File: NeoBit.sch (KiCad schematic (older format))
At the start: 19 parts, among them J1 AudioJack3_Ground, J2 Barrel_Jack_MountingPin, J3 Qwiic, J4 DotStars, J5 microbit_edge_connector, J6 NeoPixels, U1 74AHCT125, U2 MCP1702-3302E_TO92, U3 MCP1702-5002E_TO92

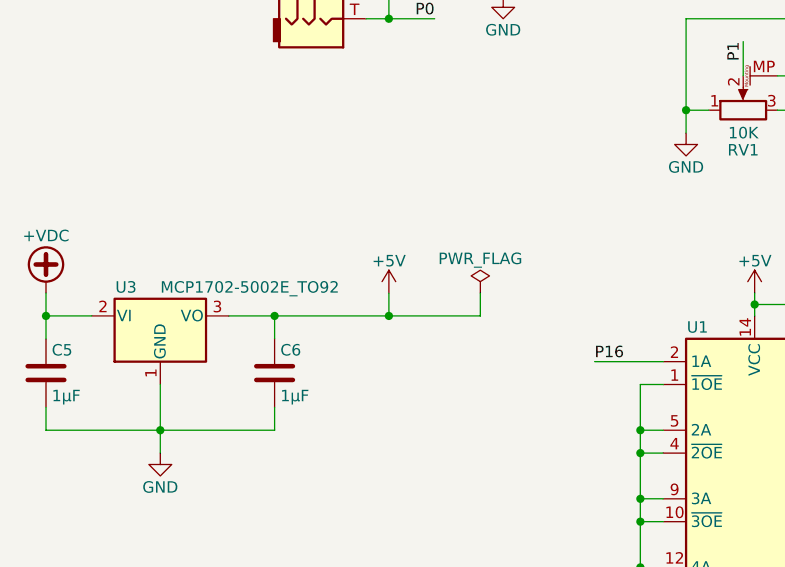
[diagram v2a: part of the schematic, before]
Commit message: Don't need this power flag.
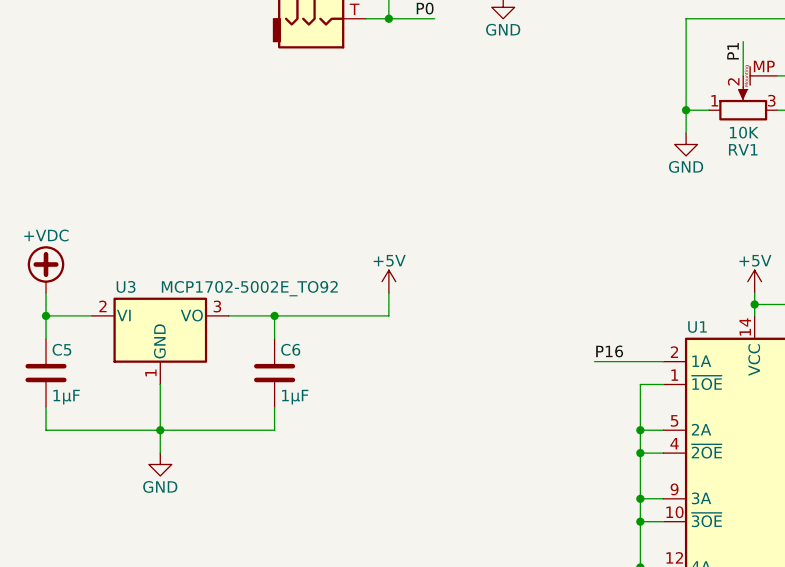
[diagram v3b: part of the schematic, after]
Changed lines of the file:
@@
 Connection ~ 1600 4100
-Wire Wire Line
-	2400 4100 3500 4100
 Wire Wire Line
 	3100 4100 3100 4000
@@
 	2100 4400 2100 4700
 Connection ~ 2100 4600
-$Comp
-L PWR_FLAG #FLG023
-U 1 1 5BA33AB3
-P 3500 4000
-F 0 "#FLG023" H 3500 4075 50  0001 C CNN
-F 1 "PWR_FLAG" H 3500 4150 50  0000 C CNN
-F 2 "" H 3500 4000 50  0001 C CNN
-F 3 "" H 3500 4000 50  0001 C CNN
-	1    3500 4000
-	1    0    0    -1
-$EndComp
-Wire Wire Line
-	3500 4100 3500 4000
-Connection ~ 3100 4100
 $Comp
 L Screw_Terminal_01x03 J6
@@
 Wire Wire Line
 	7000 3700 7200 3700
+Wire Wire Line
+	2400 4100 3100 4100
 $EndSCHEMATC

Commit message: Associate some footprints.
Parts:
- J1: footprint (none) -> footprints:SJ1-3533NG
- J3: footprint (none) -> Connectors_JST:JST_SH_SM04B-SRSS-TB_04x1.00mm_Angled
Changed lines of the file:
@@
 $EndComp
 $Comp
-L +VDC #PWR024
+L +VDC #PWR023
 U 1 1 5BA4005E
 P 5200 1400
-F 0 "#PWR024" H 5200 1300 50  0001 C CNN
+F 0 "#PWR023" H 5200 1300 50  0001 C CNN
 F 1 "+VDC" H 5200 1650 50  0000 C CNN
 F 2 "" H 5200 1400 50  0001 C CNN
@@
 $EndComp
 $Comp
-L GND #PWR025
+L GND #PWR024
 U 1 1 5BA4009C
 P 5200 1900
-F 0 "#PWR025" H 5200 1650 50  0001 C CNN
+F 0 "#PWR024" H 5200 1650 50  0001 C CNN
 F 1 "GND" H 5200 1750 50  0000 C CNN
 F 2 "" H 5200 1900 50  0001 C CNN
@@
 F 0 "J3" H 3900 1800 50  0000 C CNN
 F 1 "Qwiic" H 3900 1300 50  0000 C CNN
-F 2 "" H 3900 1600 50  0001 C CNN
+F 2 "Connectors_JST:JST_SH_SM04B-SRSS-TB_04x1.00mm_Angled" H 3900 1600 50  0001 C CNN
 F 3 "" H 3900 1600 50  0001 C CNN
 	1    3900 1600
@@
 $EndComp
 $Comp
-L GND #PWR026
+L GND #PWR025
 U 1 1 5BA3FE93
 P 3200 1600
-F 0 "#PWR026" H 3200 1350 50  0001 C CNN
+F 0 "#PWR025" H 3200 1350 50  0001 C CNN
 F 1 "GND" H 3200 1450 50  0000 C CNN
 F 2 "" H 3200 1600 50  0001 C CNN
@@
 	3200 1500 3700 1500
 $Comp
-L +3V3 #PWR027
+L +3V3 #PWR026
 U 1 1 5BA3FF8D
 P 3600 1300
-F 0 "#PWR027" H 3600 1150 50  0001 C CNN
+F 0 "#PWR026" H 3600 1150 50  0001 C CNN
 F 1 "+3V3" H 3600 1440 50  0000 C CNN
 F 2 "" H 3600 1300 50  0001 C CNN
@@
 F 0 "J1" H 2800 3050 50  0000 C CNN
 F 1 "AudioJack3_Ground" H 2800 2950 50  0000 C CNN
-F 2 "" H 2800 2700 50  0001 C CNN
+F 2 "footprints:SJ1-3533NG" H 2800 2700 50  0001 C CNN
 F 3 "" H 2800 2700 50  0001 C CNN
 F 4 "SJ1-3523N" H 2800 2700 60  0001 C CNN "MPN"
@@
 $EndComp
 $Comp
-L GND #PWR028
+L GND #PWR027
 U 1 1 5BA40629
 P 3600 2700
-F 0 "#PWR028" H 3600 2450 50  0001 C CNN
+F 0 "#PWR027" H 3600 2450 50  0001 C CNN
 F 1 "GND" H 3600 2550 50  0000 C CNN
 F 2 "" H 3600 2700 50  0001 C CNN

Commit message: Associate terminal block footprints.
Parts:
- J4: footprint (none) -> footprints:TerminalBlock_4Ucon_1x04_P3.50mm_Vertical
- J6: footprint (none) -> footprints:TerminalBlock_4Ucon_1x03_P3.50mm_Vertical
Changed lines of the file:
@@
 F 0 "J6" H 6500 5000 50  0000 C CNN
 F 1 "NeoPixels" H 6500 4600 50  0000 C CNN
-F 2 "" H 6500 4800 50  0001 C CNN
+F 2 "footprints:TerminalBlock_4Ucon_1x03_P3.50mm_Vertical" H 6500 4800 50  0001 C CNN
 F 3 "" H 6500 4800 50  0001 C CNN
 	1    6500 4800
@@
 F 0 "J4" H 5600 1800 50  0000 C CNN
 F 1 "DotStars" H 5600 1300 50  0000 C CNN
-F 2 "" H 5600 1600 50  0001 C CNN
+F 2 "footprints:TerminalBlock_4Ucon_1x04_P3.50mm_Vertical" H 5600 1600 50  0001 C CNN
 F 3 "" H 5600 1600 50  0001 C CNN
 	1    5600 1600

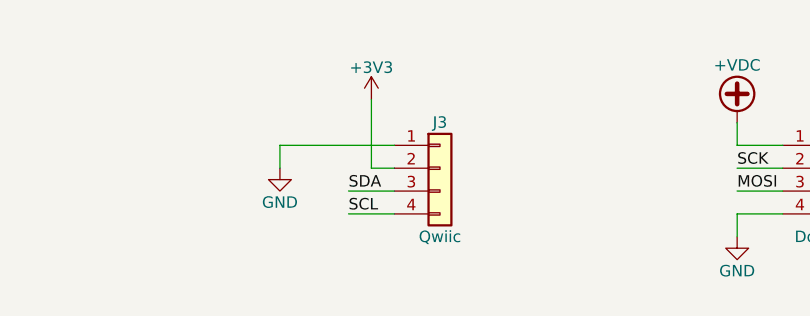
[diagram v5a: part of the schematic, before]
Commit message: Change some part numbers.
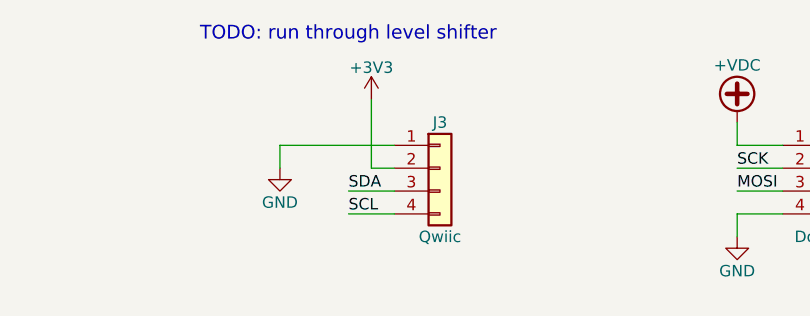
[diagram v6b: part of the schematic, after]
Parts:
- D1: footprint Diodes_THT:D_DO-15_P10.16mm_Horizontal -> Diodes_THT:D_DO-41_SOD81_P7.62mm_Horizontal; Description DIODE SCHOTTKY 40V 2A DO15 -> DIODE SCHOTTKY 20V 1A DO41; Digi-Key_PN 1655-1519-1-ND -> 1N5817FSCT-ND; MPN SB240TA -> 1N5817
- J1: Digi-Key_PN CP1-3523N-ND -> CP1-3533NG-ND; MPN SJ1-3523N -> SJ1-3533NG
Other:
- note added: "TODO: run through level shifter"
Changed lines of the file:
@@
 Sheet 1 1
 Title "Neopixel and potentiometer adapter for Micro:Bit"
-Date "2017-09-03"
-Rev "1.0"
+Date "2017-09-21"
+Rev "1.1"
 Comp "Patrick Pelletier"
 Comment1 ""
@@
 F 0 "D1" H 7200 6200 50  0000 C CNN
 F 1 "D_Schottky" H 7200 6000 50  0000 C CNN
-F 2 "Diodes_THT:D_DO-15_P10.16mm_Horizontal" H 7200 6100 50  0001 C CNN
+F 2 "Diodes_THT:D_DO-41_SOD81_P7.62mm_Horizontal" H 7200 6100 50  0001 C CNN
 F 3 "" H 7200 6100 50  0001 C CNN
-F 4 "SB240TA" H 7200 6100 60  0001 C CNN "MPN"
-F 5 "DIODE SCHOTTKY 40V 2A DO15" H 7200 6100 60  0001 C CNN "Description"
-F 6 "1655-1519-1-ND" H 7200 6100 60  0001 C CNN "Digi-Key_PN"
+F 4 "1N5817" H 7200 6100 60  0001 C CNN "MPN"
+F 5 "DIODE SCHOTTKY 20V 1A DO41" H 7200 6100 60  0001 C CNN "Description"
+F 6 "1N5817FSCT-ND" H 7200 6100 60  0001 C CNN "Digi-Key_PN"
 	1    7200 6100
 	-1   0    0    -1
@@
 F 2 "footprints:SJ1-3533NG" H 2800 2700 50  0001 C CNN
 F 3 "" H 2800 2700 50  0001 C CNN
-F 4 "SJ1-3523N" H 2800 2700 60  0001 C CNN "MPN"
+F 4 "SJ1-3533NG" H 2800 2700 60  0001 C CNN "MPN"
 F 5 "CONN JACK STEREO 3.5MM R/A" H 2800 2700 60  0001 C CNN "Description"
-F 6 "CP1-3523N-ND" H 2800 2700 60  0001 C CNN "Digi-Key_PN"
+F 6 "CP1-3533NG-ND" H 2800 2700 60  0001 C CNN "Digi-Key_PN"
 	1    2800 2700
 	1    0    0    -1
@@
 Wire Wire Line
 	2400 4100 3100 4100
+Text Notes 2850 1050 0    60   ~ 0
+TODO: run through level shifter
 $EndSCHEMATC

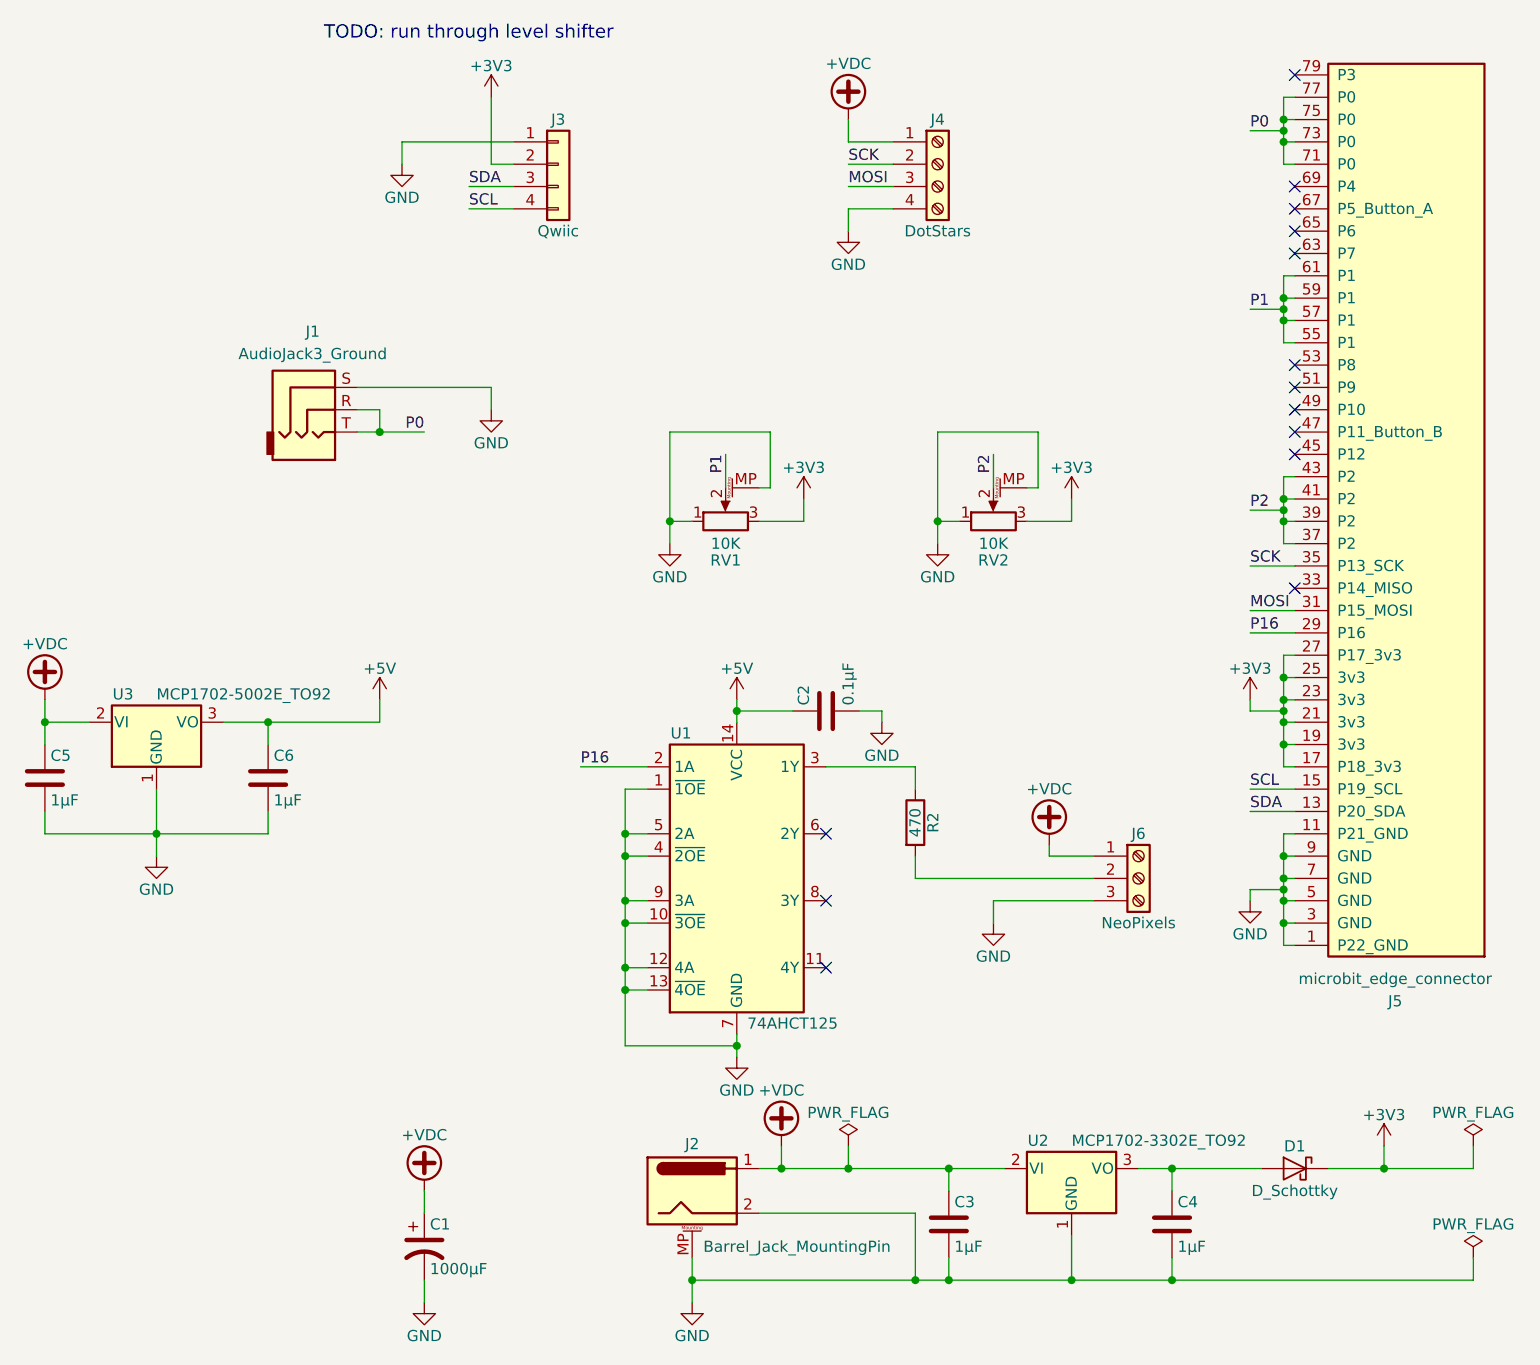
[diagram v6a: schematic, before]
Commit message: Add level shifting on DotStar pins.
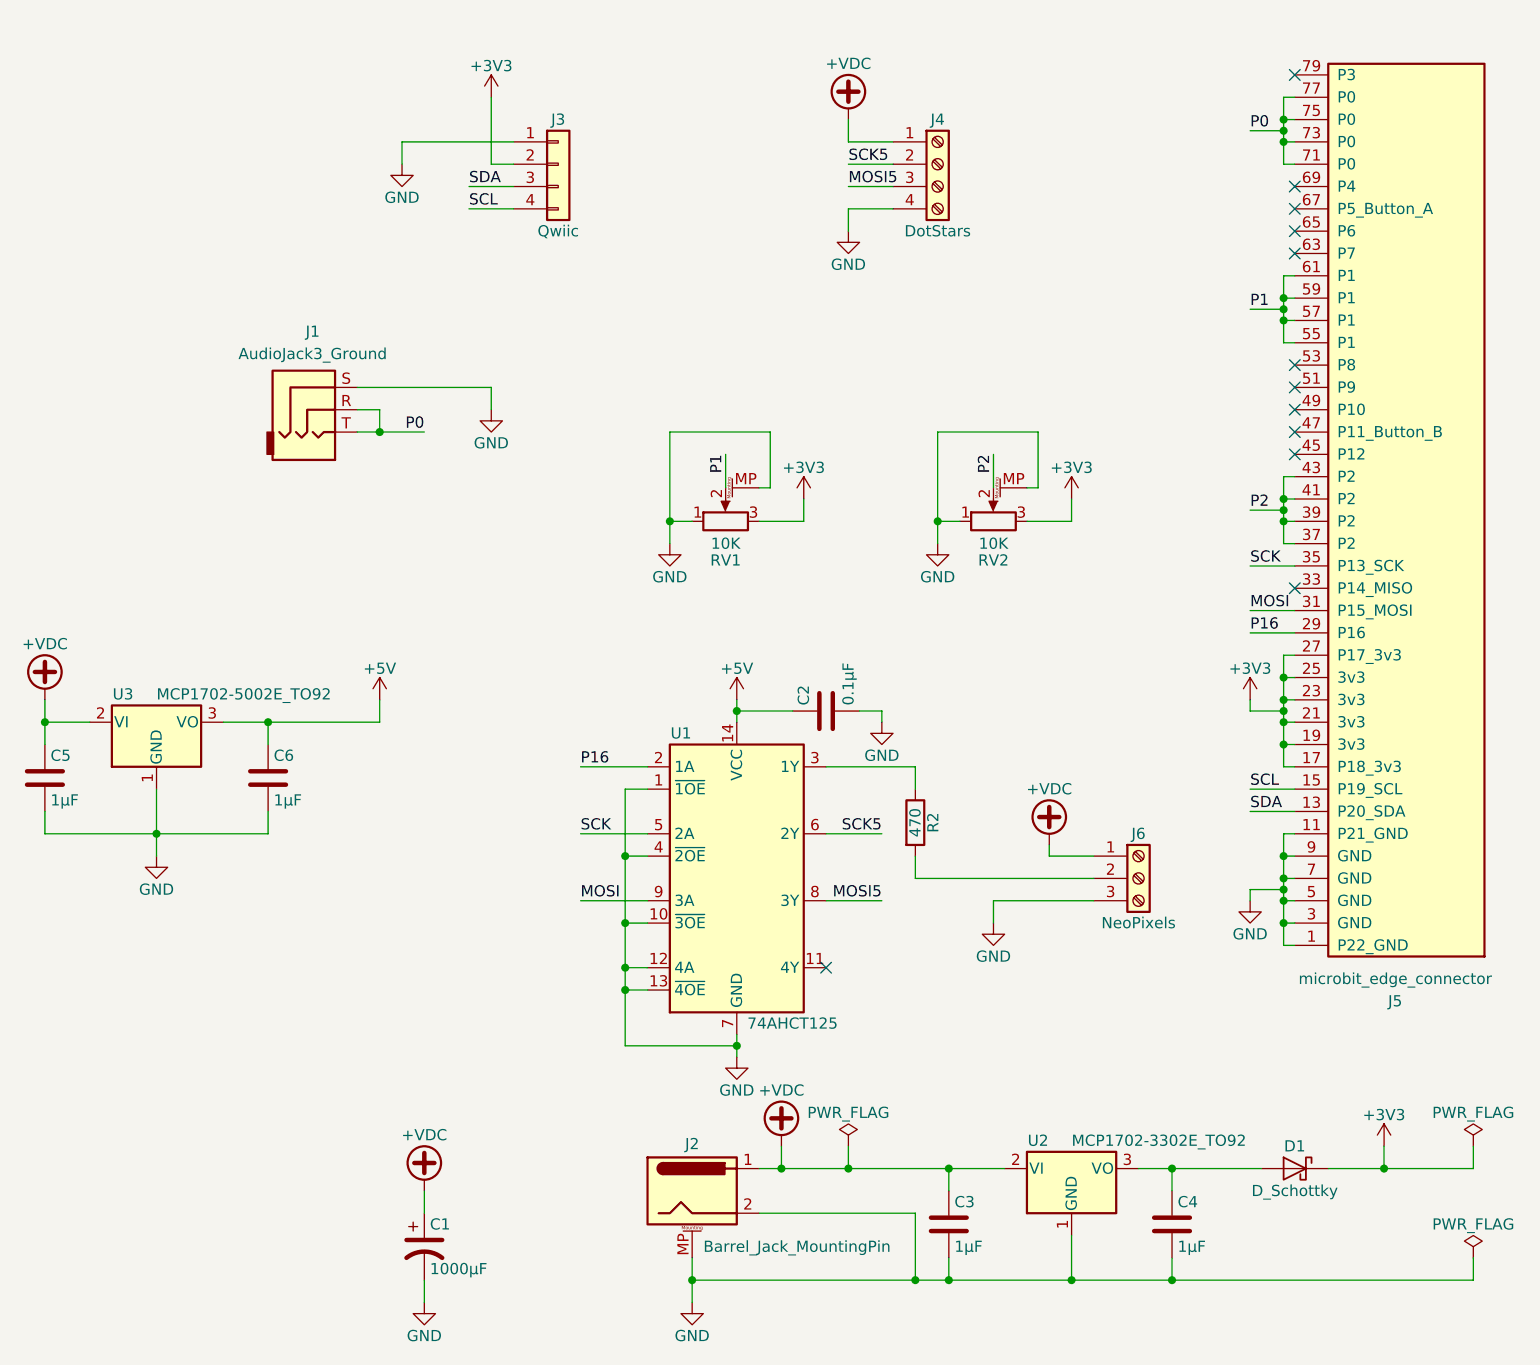
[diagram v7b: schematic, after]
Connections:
- net GND: no longer U1.5 (2A), U1.9 (3A)
- net MOSI: now also U1.9 (3A); no longer J4.3 (Pin_3)
- net SCK: now also U1.5 (2A); no longer J4.2 (Pin_2)
- net SCK5: now reaches U1.6 (2Y)
- net SCK5: now also J4.2 (Pin_2)
- net MOSI5: now reaches U1.8 (3Y)
- net MOSI5: now also J4.3 (Pin_3)
- no-connect marks 14 -> 12
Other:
- note removed: "TODO: run through level shifter"
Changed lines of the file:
@@
 Connection ~ 4700 5550
-Wire Wire Line
-	4300 4600 4200 4600
-Connection ~ 4200 4600
 Wire Wire Line
 	4300 4700 4200 4700
 Connection ~ 4200 4700
-Wire Wire Line
-	4300 4900 4200 4900
-Connection ~ 4200 4900
 Wire Wire Line
 	4300 5000 4200 5000
@@
 Wire Wire Line
 	4000 4300 4300 4300
-NoConn ~ 5100 4600
-NoConn ~ 5100 4900
 NoConn ~ 5100 5200
 $Comp
@@
 $EndComp
 Text Label 5200 1600 0    50   ~ 0
-SCK
+SCK5
 Text Label 5200 1700 0    50   ~ 0
-MOSI
+MOSI5
 Wire Wire Line
 	5200 1400 5200 1500
@@
 Wire Wire Line
 	2400 4100 3100 4100
-Text Notes 2850 1050 0    60   ~ 0
-TODO: run through level shifter
+Text Label 4000 4600 0    50   ~ 0
+SCK
+Text Label 4000 4900 0    50   ~ 0
+MOSI
+Wire Wire Line
+	4000 4600 4300 4600
+Wire Wire Line
+	4000 4900 4300 4900
+Text Label 5350 4600 2    50   ~ 0
+SCK5
+Text Label 5350 4900 2    50   ~ 0
+MOSI5
+Wire Wire Line
+	5100 4600 5350 4600
+Wire Wire Line
+	5100 4900 5350 4900
 $EndSCHEMATC

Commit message: Use a higher-voltage capacitor.
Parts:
- C1: Description CAP ALUM 1000UF 20% 10V RADIAL -> CAP ALUM 1000UF 20% 25V RADIAL; Digi-Key_PN 1189-3703-1-ND -> 1189-1583-1-ND; MPN 10WXA1000MEFCT810X9 -> 25PX1000MEFCT810X16
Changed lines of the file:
@@
 F 2 "Capacitors_THT:CP_Radial_D10.0mm_P5.00mm" H 3300 6450 50  0001 C CNN
 F 3 "" H 3300 6450 50  0001 C CNN
-F 4 "10WXA1000MEFCT810X9" H 3300 6450 60  0001 C CNN "MPN"
-F 5 "CAP ALUM 1000UF 20% 10V RADIAL" H 3300 6450 60  0001 C CNN "Description"
-F 6 "1189-3703-1-ND" H 3300 6450 60  0001 C CNN "Digi-Key_PN"
+F 4 "25PX1000MEFCT810X16" H 3300 6450 60  0001 C CNN "MPN"
+F 5 "CAP ALUM 1000UF 20% 25V RADIAL" H 3300 6450 60  0001 C CNN "Description"
+F 6 "1189-1583-1-ND" H 3300 6450 60  0001 C CNN "Digi-Key_PN"
 	1    3300 6450
 	1    0    0    -1
